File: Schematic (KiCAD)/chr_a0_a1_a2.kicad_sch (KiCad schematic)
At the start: 23 parts, among them P27 INVERT

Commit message: - Started work on the pulse channels.  - Solved at least 2 of the red traces in the SVG.  - Finally realized that "Unknown 4to1" cells are actually just ordinary And-Or-Invert "AOI22" cells.
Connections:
- net at R15. (X): now also R16. (X); no longer R3. (X)
- net at P27. (X): now also N18,19,20,21,24,25,27,29,32,34,36,37. (Y3), N22. (X), N28. (X); no longer R25. (X)
- net at N14. (X): now also N22. (X), N26. (X); no longer N11,12,13. (/Q1)
- net at N7. (X): now also N10. (X), N8. (X); no longer N6. (X)
- net at N28. (X): now also N26. (X); no longer N18,19,20,21,24,25,27,29,32,34,36,37. (Y3)
- new net: R15. (X), R16. (X), R17,18,19,20,21,22,23. (/Q2)
- new net: R15. (X), R3. (X)
- new net: N3. (X), N4. (X), N5. (X)
- new net: N3. (X), N4. (X)
- new net: P27. (X), R25. (X)
- new net: N11,12,13. (/Q1), N14. (X)
- new net: N11,12,13. (/Q1), N8. (X)
- new net: N5. (X), N6. (X)
- new net: N6. (X), N7. (X)
- new net: R17,18,19,20,21,22,23. (/Q2), R25. (X)
- new net: N18,19,20,21,24,25,27,29,32,34,36,37. (Y3), N28. (X)
- new net: N18,19,20,21,24,25,27,29,32,34,36,37. (Y3), N23. (X)
- new net: N17. (X), N18,19,20,21,24,25,27,29,32,34,36,37. (Y3)
- new net: N18,19,20,21,24,25,27,29,32,34,36,37. (Y3), N30. (X)
- new net: N10. (X), N15. (X)

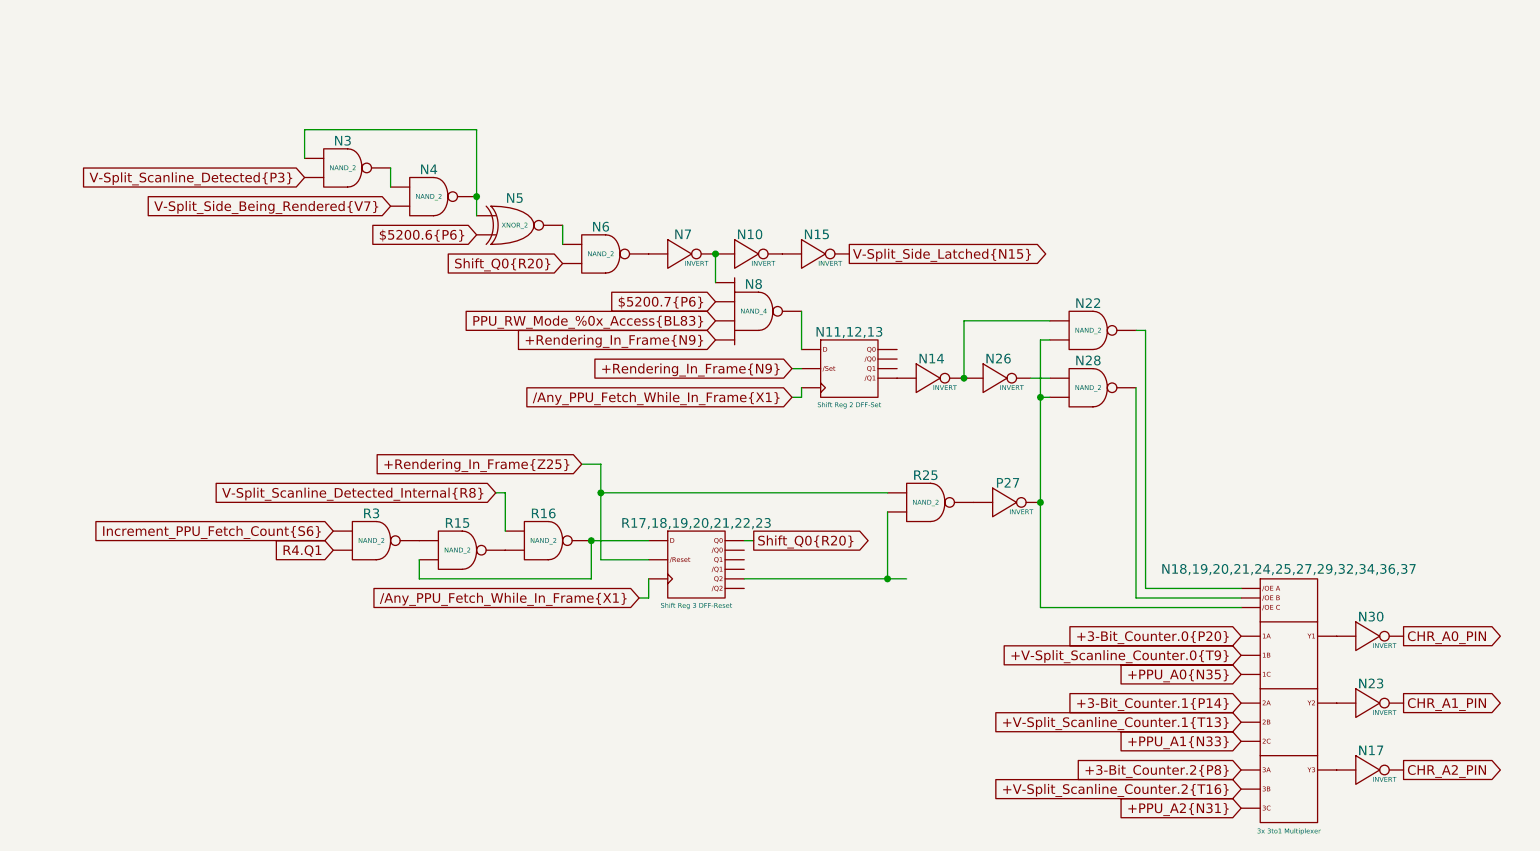
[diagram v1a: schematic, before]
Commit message: Schematic Updates:  - Added all 10-bit CHR banking registers $5120 - $512B, including where all 10 bits come from when written.  - Added 8-bit CHR bank register $5202, which is the bank used when rendering the V-Split region.    + V-Split seems to always be 8-bit, 8kB bank regardless of CHR mode.  The wiki doesn't say that and I don't know for sure.  - Added decoding logic that activates the correct CHR bank for CHR A10, A11, A12 (corresponding to columns AV, AW, AX).  - Noted, AX15 activates $5202 CHR Bank for V-Split region.  AX16 activates CHR Bank from data stored in ExRAM for extended attributes.  Therefore, AX15 driven by AT1 High means we specifically are in v-split region, and not extended attribute mode.  With this knowledge, backtracking up the chain from AT1 to N14 sheds very useful insight what the 3-bit shift register at N11/N12/N13 is doing.  We now know that N14 goes low specifically for pattern table fetches when rendering the V-split region, and does not appear dual-purposed for extended attribute fetch sequencing.  This may seem rather subtle or unimportant, but it is a good advancement for higher level understanding what that mysterious shift register might be doing.
SVG Trace Updates:
 - Registers $5120, 5121, 5122, 5123 (first 4 CHR bank register), the outputs were labeled in reverse order.
 - Register $5130 (highest CHR bank bits), the outputs were labeled with backwards polarity.  The error was not having taken into account that the CPU data bus input to the latches came already inverted to begin with.
 - Still wrong: Cell AV7, 2-input NAND gate.  One of the inputs is missing and it logically should be driven by AS19 like the 4 cells to its direct right.  I can't quite make out how it makes that connection.
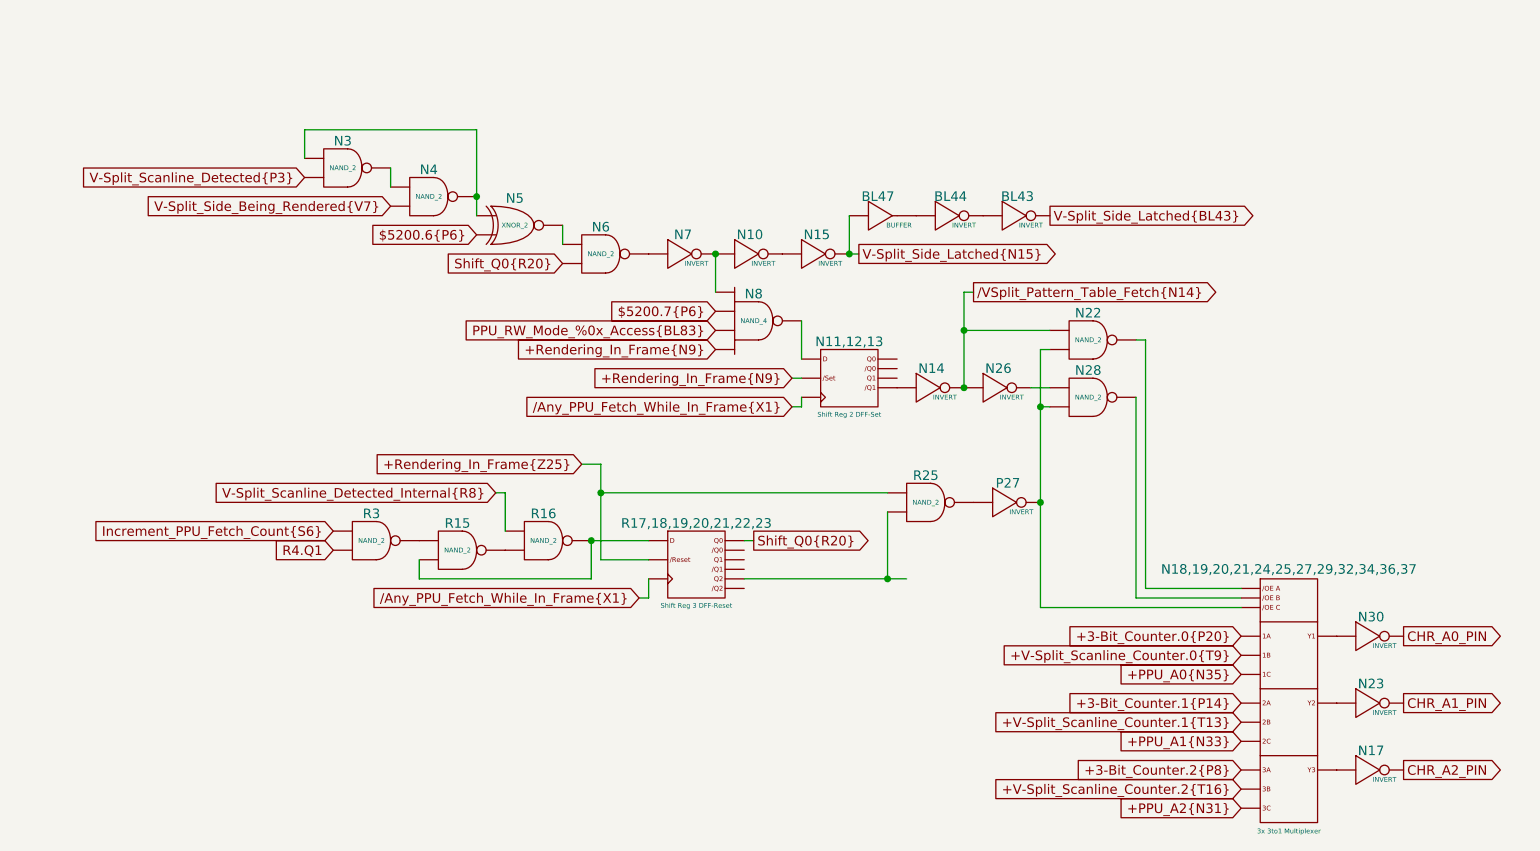
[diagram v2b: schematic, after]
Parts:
- added BL43, BL44: INVERT, symbol MMC5:INVERT
- added BL47: BUFFER, symbol MMC5:BUFFER
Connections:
- net V-Split_Side_Latched{N15}: now also BL47. (X)
- net at R15. (X): now also R16. (X); no longer R3. (X)
- net at P27. (X): now also N18,19,20,21,24,25,27,29,32,34,36,37. (Y3), N22. (X), N28. (X); no longer R25. (X)
- net /VSplit_Pattern_Table_Fetch{N14}: now reaches N14. (X)
- net /VSplit_Pattern_Table_Fetch{N14}: now also N22. (X), N26. (X); no longer N11,12,13. (/Q1)
- net at N7. (X): now also N10. (X), N8. (X); no longer N6. (X)
- net at N28. (X): now also N26. (X); no longer N18,19,20,21,24,25,27,29,32,34,36,37. (Y3)
- new net: R15. (X), R16. (X), R17,18,19,20,21,22,23. (/Q2)
- new net: R15. (X), R3. (X)
- new net: N3. (X), N4. (X), N5. (X)
- new net: N3. (X), N4. (X)
- new net: P27. (X), R25. (X)
- new net: N11,12,13. (/Q1), N14. (X)
- new net: N11,12,13. (/Q1), N8. (X)
- new net: N5. (X), N6. (X)
- new net: N6. (X), N7. (X)
- new net: BL44. (X), BL47. (X)
- new net: R17,18,19,20,21,22,23. (/Q2), R25. (X)
- new net: N18,19,20,21,24,25,27,29,32,34,36,37. (Y3), N28. (X)
- new net: N18,19,20,21,24,25,27,29,32,34,36,37. (Y3), N23. (X)
- new net: BL43. (X), BL44. (X)
- new net: N17. (X), N18,19,20,21,24,25,27,29,32,34,36,37. (Y3)
- new net: N18,19,20,21,24,25,27,29,32,34,36,37. (Y3), N30. (X)
- new net: N18,19,20,21,24,25,27,29,32,34,36,37. (Y3), N22. (X)
- new net: N10. (X), N15. (X)
- new net V-Split_Side_Latched{BL43}: BL43. (X)
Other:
- moved on the sheet: N11,12,13, N14, N22, N26, N28, N8

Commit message: - All cells in the left and center areas have now been added into the schematics.  - Changed naming of the PDF files; I was accidentally writing over furrtek's original with my new PDF.
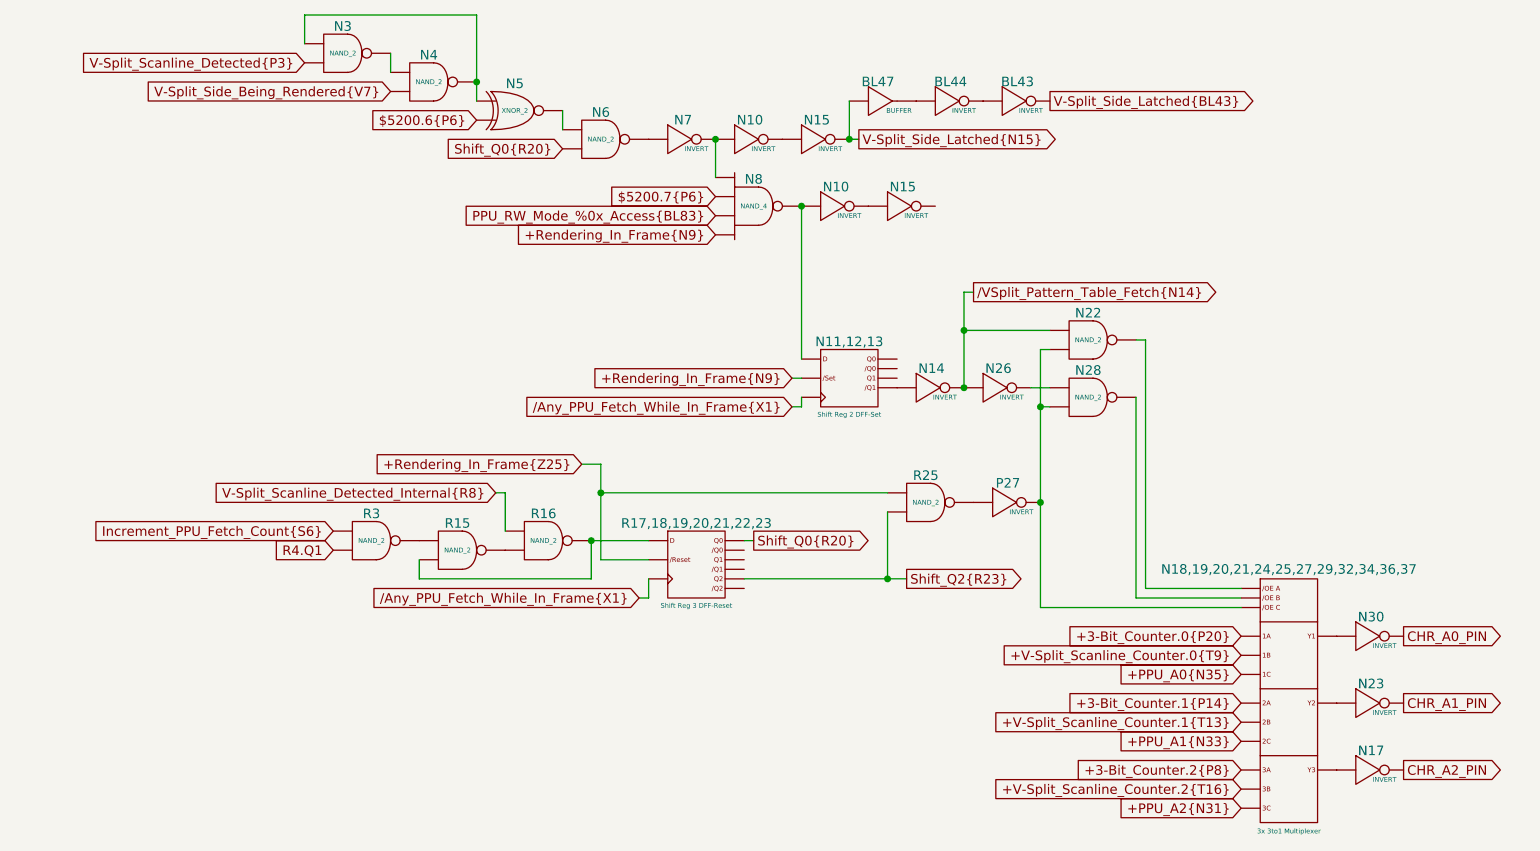
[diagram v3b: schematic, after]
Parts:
- added N10, N15: INVERT, symbol MMC5:INVERT
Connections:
- net at R15. (X): now also R16. (X); no longer R3. (X)
- net at P27. (X): now also N18,19,20,21,24,25,27,29,32,34,36,37. (Y3), N22. (X), N28. (X); no longer R25. (X)
- net at N7. (X): now also N10. (X), N8. (X); no longer N6. (X)
- net at BL44. (X): now also BL43. (X); no longer BL47. (X)
- net Shift_Q2{R23}: now reaches R17,18,19,20,21,22,23. (/Q2), R25. (X)
- net at N28. (X): now also N26. (X); no longer N18,19,20,21,24,25,27,29,32,34,36,37. (Y3)
- new net: R15. (X), R16. (X), R17,18,19,20,21,22,23. (/Q2)
- new net: R15. (X), R3. (X)
- new net: N3. (X), N4. (X), N5. (X)
- new net: N3. (X), N4. (X)
- new net: P27. (X), R25. (X)
- new net: N10. (X), N11,12,13. (/Q1), N8. (X)
- new net: N11,12,13. (/Q1), N14. (X)
- new net: N5. (X), N6. (X)
- new net: N6. (X), N7. (X)
- new net: BL44. (X), BL47. (X)
- new net: N18,19,20,21,24,25,27,29,32,34,36,37. (Y3), N28. (X)
- new net: N18,19,20,21,24,25,27,29,32,34,36,37. (Y3), N23. (X)
- new net: N10. (X), N15. (X) (x2)
- new net: N17. (X), N18,19,20,21,24,25,27,29,32,34,36,37. (Y3)
- new net: N18,19,20,21,24,25,27,29,32,34,36,37. (Y3), N30. (X)
- new net: N18,19,20,21,24,25,27,29,32,34,36,37. (Y3), N22. (X)
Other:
- moved on the sheet: BL43, BL44, BL47, N10, N15, N3, N4, N5, N6, N7, N8
